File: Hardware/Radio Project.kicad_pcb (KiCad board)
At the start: 10 copper layers, 100 x 70 mm, 110 parts, among them J1 FTSH-105-X-X-DV-007-P-X, J2 USB_C_Receptacle, J3 132225, J4 132225, J5 WE-RJ45_7499010211A, SW1 208-4, U1 STM32F407VGT6, U2 SIT1566AC-JV-XXE-32.768D, U3 ADP2164ACPZ-3.3-R7, U4 SI4468-A2A-IM, U5 SI4468-A2A-IM, U6 DP83822IRHBR, Y1 TG2520SMN 30.0000M-MCGNNM0, Y2 TG2520SMN 30.0000M-MCGNNM0

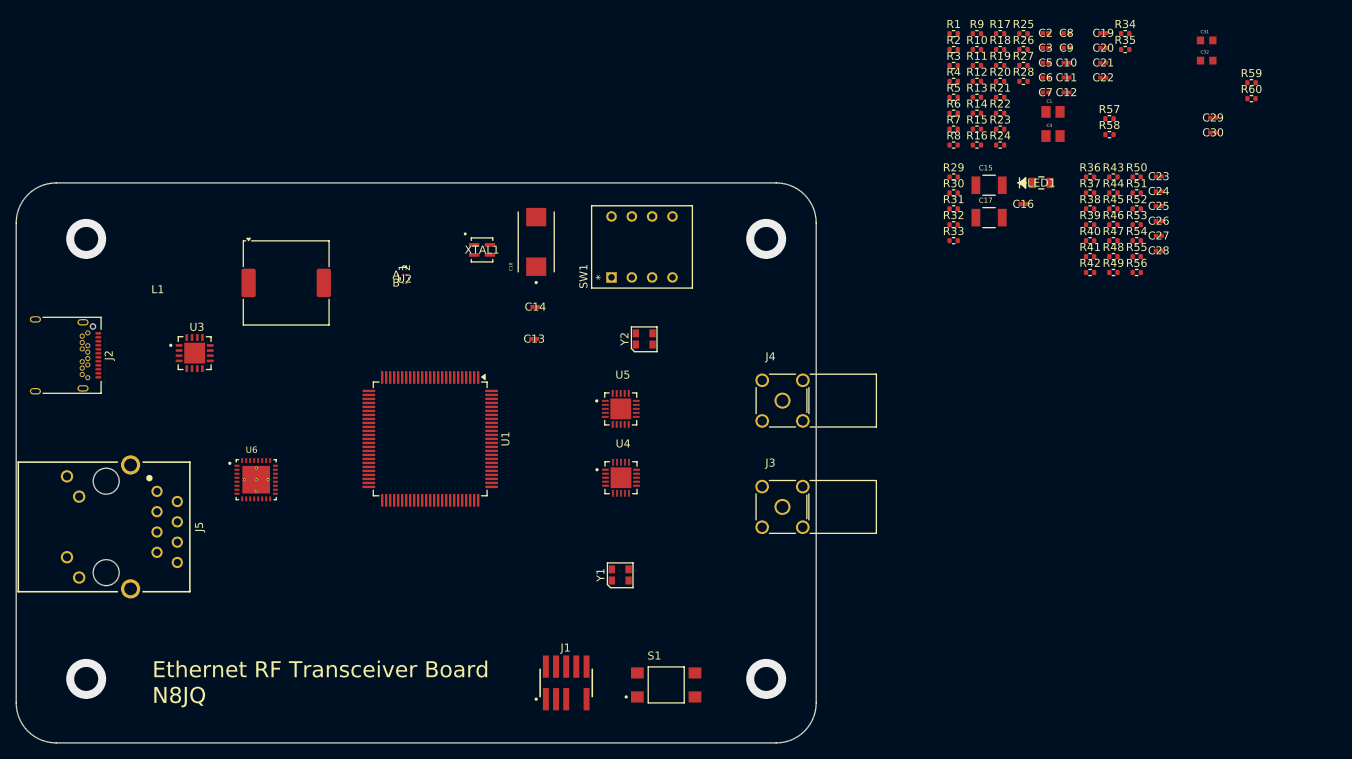
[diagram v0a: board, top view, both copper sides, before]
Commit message: added RF matching network and added all 16 layers to stackup
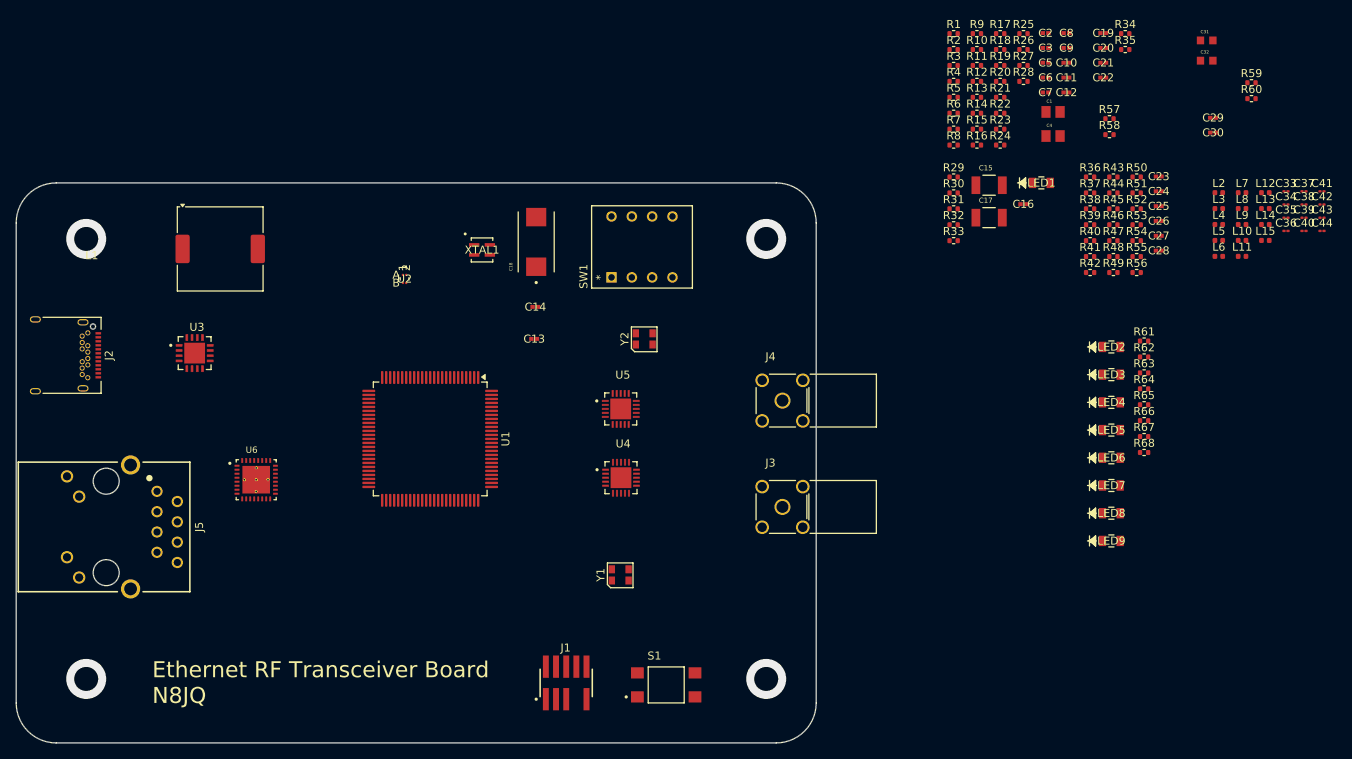
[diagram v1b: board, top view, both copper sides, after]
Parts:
- added C33: 3.3pF, Capacitor_SMD:C_01005_0402Metric, F.Cu at (255.0, 49.0)
- added C34: 3.3pF, Capacitor_SMD:C_01005_0402Metric, F.Cu at (255.0, 50.7)
- added C35: 4.7pF, Capacitor_SMD:C_01005_0402Metric, F.Cu at (255.0, 52.4)
- added C36: 1pF, Capacitor_SMD:C_01005_0402Metric, F.Cu at (255.0, 54.0)
- added C37: 3pF, Capacitor_SMD:C_01005_0402Metric, F.Cu at (257.2, 49.0)
- added C38: 6.2nF, Capacitor_SMD:C_01005_0402Metric, F.Cu at (257.2, 50.7)
- added C39: 3pF, Capacitor_SMD:C_01005_0402Metric, F.Cu at (257.2, 52.4)
- added C40: 4.7pF, Capacitor_SMD:C_01005_0402Metric, F.Cu at (257.2, 54.0)
- added C41: 1pF, Capacitor_SMD:C_01005_0402Metric, F.Cu at (259.5, 49.0)
- added C42: 6.2nF, Capacitor_SMD:C_01005_0402Metric, F.Cu at (259.5, 50.7)
- added C43: 3.3pF, Capacitor_SMD:C_01005_0402Metric, F.Cu at (259.5, 52.4)
- added C44: 3.3pF, Capacitor_SMD:C_01005_0402Metric, F.Cu at (259.5, 54.0)
- added L10: 18nH, Inductor_SMD:L_0402_1005Metric, F.Cu at (249.5, 55.2)
- added L11: 22nH, Inductor_SMD:L_0402_1005Metric, F.Cu at (249.5, 57.2)
- added L12: 3.3nH, Inductor_SMD:L_0402_1005Metric, F.Cu at (252.4, 49.2)
- added L13: 11nH, Inductor_SMD:L_0402_1005Metric, F.Cu at (252.4, 51.2)
- added L14: 22nH, Inductor_SMD:L_0402_1005Metric, F.Cu at (252.4, 53.2)
- added L15: 11nH, Inductor_SMD:L_0402_1005Metric, F.Cu at (252.4, 55.2)
- added L2: 22nH, Inductor_SMD:L_0402_1005Metric, F.Cu at (246.6, 49.2)
- added L3: 11nH, Inductor_SMD:L_0402_1005Metric, F.Cu at (246.6, 51.2)
- added L4: 100nH, Inductor_SMD:L_0402_1005Metric, F.Cu at (246.6, 53.2)
- added L5: 22nH, Inductor_SMD:L_0402_1005Metric, F.Cu at (246.6, 55.2)
- added L6: 18nH, Inductor_SMD:L_0402_1005Metric, F.Cu at (246.6, 57.2)
- added L7: 3.3nH, Inductor_SMD:L_0402_1005Metric, F.Cu at (249.5, 49.2)
- added L8: 11nH, Inductor_SMD:L_0402_1005Metric, F.Cu at (249.5, 51.2)
- added L9: 100nH, Inductor_SMD:L_0402_1005Metric, F.Cu at (249.5, 53.2)
- added LED2: CMD17-21VGD/TR8, CMD17_21VGD_TR8:LED0805N_CML-M, F.Cu at (233.1, 68.5)
- added LED3: CMD17-21VGD/TR8, CMD17_21VGD_TR8:LED0805N_CML-M, F.Cu at (233.1, 72.0)
- added LED4: CMD17-21VGD/TR8, CMD17_21VGD_TR8:LED0805N_CML-M, F.Cu at (233.1, 75.4)
- added LED5: CMD17-21VGD/TR8, CMD17_21VGD_TR8:LED0805N_CML-M, F.Cu at (233.1, 78.9)
- added LED6: CMD17-21VGD/TR8, CMD17_21VGD_TR8:LED0805N_CML-M, F.Cu at (233.1, 82.4)
- added LED7: CMD17-21VGD/TR8, CMD17_21VGD_TR8:LED0805N_CML-M, F.Cu at (233.1, 85.8)
- added LED8: CMD17-21VGD/TR8, CMD17_21VGD_TR8:LED0805N_CML-M, F.Cu at (233.1, 89.3)
- added LED9: CMD17-21VGD/TR8, CMD17_21VGD_TR8:LED0805N_CML-M, F.Cu at (233.1, 92.8)
- added R61: 60, Resistor_SMD:R_0402_1005Metric, F.Cu at (237.2, 67.8)
- added R62: 60, Resistor_SMD:R_0402_1005Metric, F.Cu at (237.2, 69.8)
- added R63: 60, Resistor_SMD:R_0402_1005Metric, F.Cu at (237.2, 71.7)
- added R64: 60, Resistor_SMD:R_0402_1005Metric, F.Cu at (237.2, 73.7)
- added R65: 60, Resistor_SMD:R_0402_1005Metric, F.Cu at (237.2, 75.7)
- added R66: 60, Resistor_SMD:R_0402_1005Metric, F.Cu at (237.2, 77.7)
- added R67: 60, Resistor_SMD:R_0402_1005Metric, F.Cu at (237.2, 79.7)
- added R68: 60, Resistor_SMD:R_0402_1005Metric, F.Cu at (237.2, 81.7)
- moved L1 9.28 mm to (121.8, 56.2)
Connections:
- J3 pad 1: RF1_SMA -> /RF Chain/RF1_SMA
- J4 pad 1: RF2_SMA -> /RF Chain/RF2_SMA
- U1 pad 55: unconnected-(U1-PD8-Pad55) -> Net-(U1-PD8)
- U1 pad 56: unconnected-(U1-PD9-Pad56) -> Net-(U1-PD9)
- U1 pad 83: unconnected-(U1-PD2-Pad83) -> Net-(U1-PD2)
- U1 pad 84: unconnected-(U1-PD3-Pad84) -> Net-(U1-PD3)
- U1 pad 85: unconnected-(U1-PD4-Pad85) -> Net-(U1-PD4)
- U1 pad 86: unconnected-(U1-PD5-Pad86) -> Net-(U1-PD5)
- U1 pad 87: unconnected-(U1-PD6-Pad87) -> Net-(U1-PD6)
- U1 pad 88: unconnected-(U1-PD7-Pad88) -> Net-(U1-PD7)
- U4 pad 2: unconnected-(U4-RXP-Pad2) -> RF1_RX_P
- U4 pad 3: unconnected-(U4-RXN-Pad3) -> RF1_RX_N
- U4 pad 4: unconnected-(U4-TX-Pad4) -> RF1_TX
- U5 pad 2: unconnected-(U5-RXP-Pad2) -> RF2_RX_P
- U5 pad 3: unconnected-(U5-RXN-Pad3) -> RF2_RX_N
- U5 pad 4: unconnected-(U5-TX-Pad4) -> RF2_TX
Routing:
- added copper zone on In1.Cu, net GND
- added copper zone on In10.Cu, net GND
- added copper zone on In12.Cu, net GND
- added copper zone on In14.Cu, net GND
- added copper zone on In3.Cu, net GND
- added copper zone on In8.Cu, net GND
- removed copper zone on In2.Cu, net GND
- removed copper zone on In4.Cu, net GND
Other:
- copper layers 10 -> 16

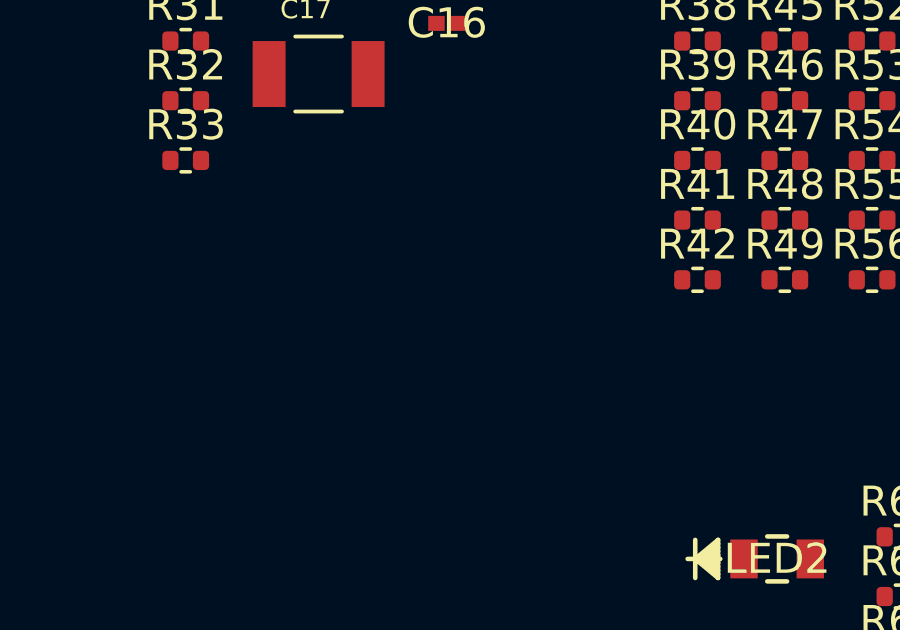
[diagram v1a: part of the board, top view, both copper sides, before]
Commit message: connected USB 2.0 data pins
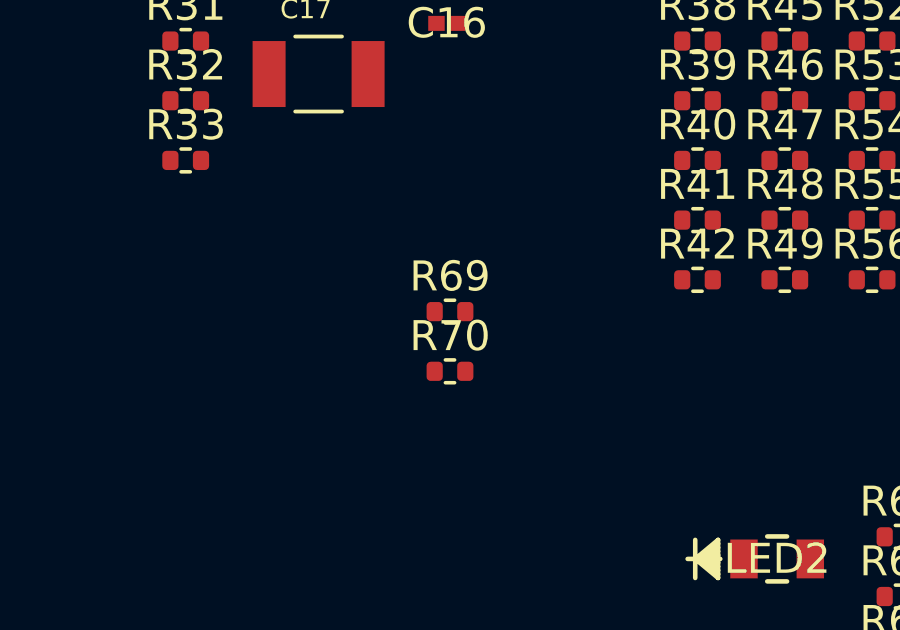
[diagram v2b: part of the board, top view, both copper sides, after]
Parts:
- added R69: 40, Resistor_SMD:R_0402_1005Metric, F.Cu at (222.2, 60.3)
- added R70: 40, Resistor_SMD:R_0402_1005Metric, F.Cu at (222.2, 62.2)
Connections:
- J2 pad A6: unconnected-(J2-D+-PadA6) -> USB_DP
- J2 pad A7: unconnected-(J2-D--PadA7) -> USB_DM
- J2 pad B6: unconnected-(J2-D+-PadB6) -> USB_DM
- J2 pad B7: unconnected-(J2-D--PadB7) -> USB_DP
- U1 pad 70: unconnected-(U1-PA11-Pad70) -> Net-(U1-PA11)
- U1 pad 71: unconnected-(U1-PA12-Pad71) -> Net-(U1-PA12)

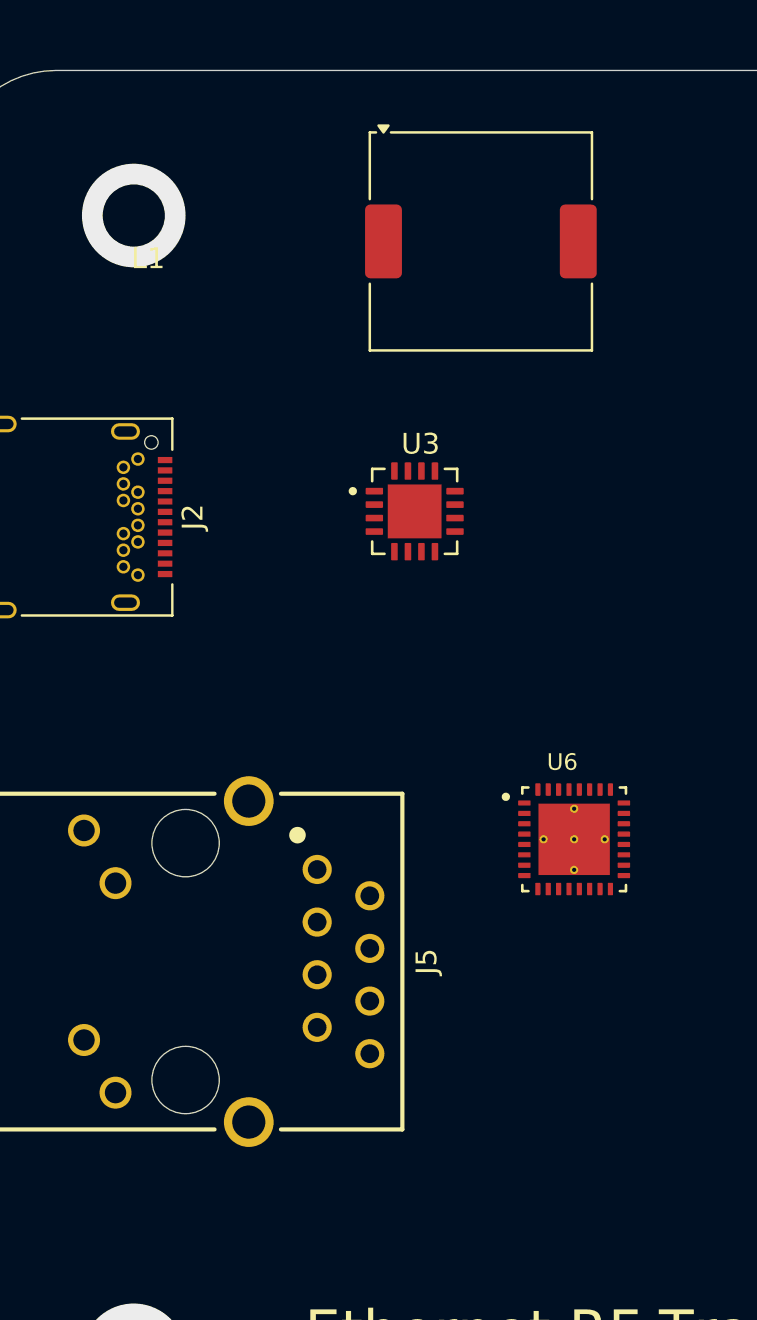
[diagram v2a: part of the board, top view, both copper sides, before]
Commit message: Added 5V plane
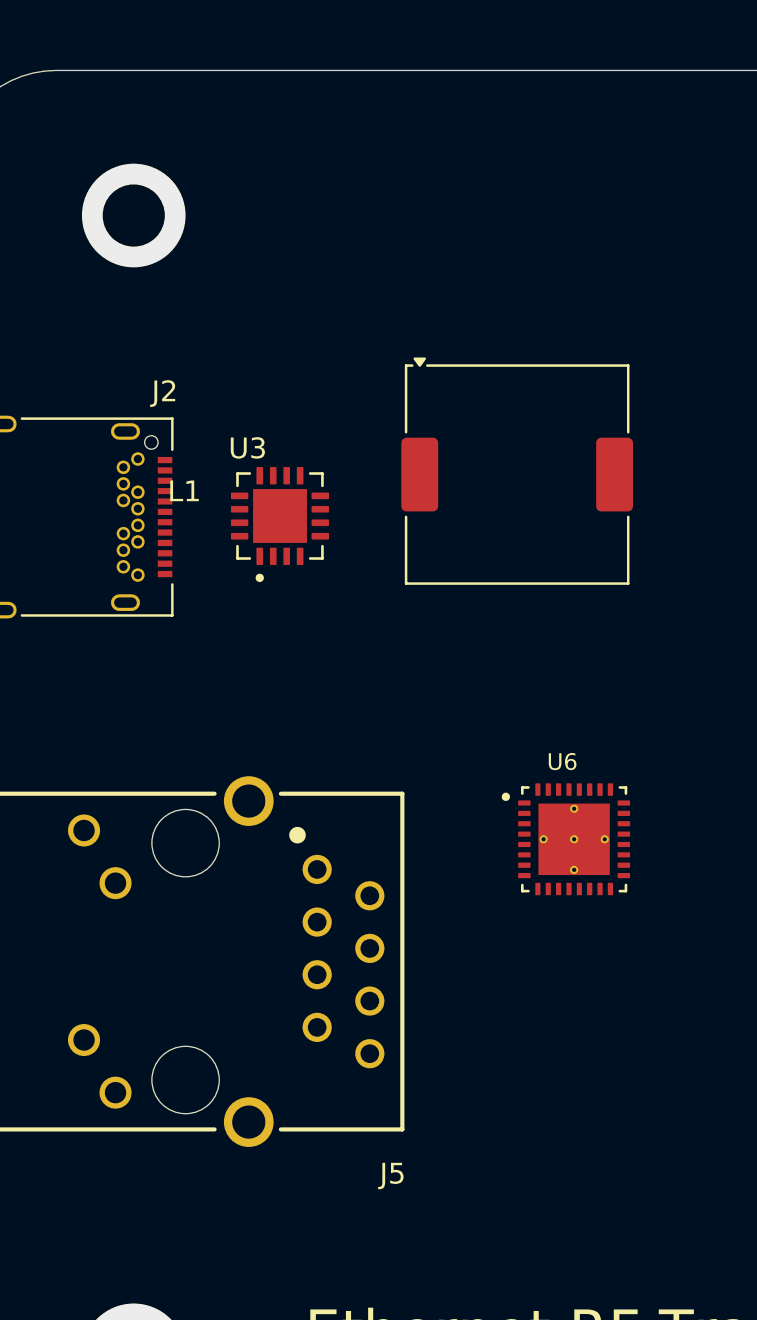
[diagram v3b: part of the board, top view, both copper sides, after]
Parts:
- moved L1 11.4 mm to (123.5, 67.5)
- moved U3 6.50 mm to (112.1, 69.5), turned to 90 degrees
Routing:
- added copper zone on In13.Cu, net +3.3V
- added copper zone on In2.Cu, net +3.3V
- added copper zone on In13.Cu, net +5V
- added copper zone on In2.Cu, net +5V
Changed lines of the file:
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@@
 		(at 107.5 91 -90)
 		(property "Reference" "J5"
-			(at 0 -11.635 90)
+			(at 10.25 -10 180)
 			(layer "F.SilkS")
 			(effects
@@
 		(tags "USB C Type-C Receptacle Hybrid")
 		(property "Reference" "J2"
-			(at 0 -6.36 90)
+			(at -6.05 -5.01 180)
 			(layer "F.SilkS")
 			(effects
@@
 	(footprint "ADP2164ACPZ_3_3_R7:QFN65P400X400X80-17N"
 		(layer "F.Cu")
-		(at 118.555 69.275)
+		(at 112.055 69.5 90)
 		(property "Reference" "U3"
-			(at 0.285 -3.25 0)
+			(at 3.25 -1.555 180)
 			(layer "F.SilkS")
 			(effects
@@
 		)
 		(property "Value" "ADP2164ACPZ-3.3-R7"
-			(at 9.81 3.25 0)
+			(at 9.81 3.25 90)
 			(layer "F.Fab")
 			(effects
@@
 		)
 		(property "Datasheet" ""
-			(at 0 0 0)
+			(at 0 0 90)
 			(layer "F.Fab")
 			(hide yes)
@@
 		)
 		(property "Description" ""
-			(at 0 0 0)
+			(at 0 0 90)
 			(layer "F.Fab")
 			(hide yes)
@@
 		(attr smd)
 		(fp_line
-			(start -2.05 -2.05)
-			(end -2.05 -1.455)
+			(start 2.05 -2.05)
+			(end 1.455 -2.05)
 			(stroke
 				(width 0.127)
@@
 		)
 		(fp_line
-			(start -2.05 -2.05)
-			(end -1.455 -2.05)
+			(start 2.05 -2.05)
+			(end 2.05 -1.455)
 			(stroke
 				(width 0.127)
@@
 		)
 		(fp_line
-			(start -2.05 2.05)
-			(end -2.05 1.455)
+			(start -2.05 -2.05)
+			(end -1.455 -2.05)
 			(stroke
 				(width 0.127)
@@
 		)
 		(fp_line
-			(start -2.05 2.05)
-			(end -1.455 2.05)
+			(start -2.05 -2.05)
+			(end -2.05 -1.455)
 			(stroke
 				(width 0.127)
@@
 		)
 		(fp_line
-			(start 2.05 -2.05)
-			(end 1.455 -2.05)
+			(start 2.05 2.05)
+			(end 2.05 1.455)
 			(stroke
 				(width 0.127)
@@
 		)
 		(fp_line
-			(start 2.05 -2.05)
-			(end 2.05 -1.455)
+			(start 2.05 2.05)
+			(end 1.455 2.05)
 			(stroke
 				(width 0.127)
@@
 		)
 		(fp_line
-			(start 2.05 2.05)
-			(end 1.455 2.05)
+			(start -2.05 2.05)
+			(end -2.05 1.455)
 			(stroke
 				(width 0.127)
@@
 		)
 		(fp_line
-			(start 2.05 2.05)
-			(end 2.05 1.455)
+			(start -2.05 2.05)
+			(end -1.455 2.05)
 			(stroke
 				(width 0.127)
@@
 		)
 		(fp_line
-			(start -2.615 2.615)
-			(end -2.615 -2.615)
+			(start 2.615 2.615)
+			(end 2.615 -2.615)
 			(stroke
 				(width 0.05)
@@
 		(fp_line
 			(start -2.615 2.615)
-			(end 2.615 2.615)
+			(end -2.615 -2.615)
 			(stroke
 				(width 0.05)
@@
 		)
 		(fp_line
-			(start 2.615 2.615)
-			(end 2.615 -2.615)
+			(start -2.615 2.615)
+			(end 2.615 2.615)
 			(stroke
 				(width 0.05)
@@
 		)
 		(fp_line
-			(start -2.05 2.05)
+			(start 2.05 -2.05)
 			(end -2.05 -2.05)
 			(stroke
@@
 		)
 		(fp_line
-			(start 2.05 -2.05)
-			(end -2.05 -2.05)
+			(start 2.05 2.05)
+			(end 2.05 -2.05)
 			(stroke
 				(width 0.127)
@@
 		)
 		(fp_line
-			(start 2.05 2.05)
-			(end 2.05 -2.05)
+			(start -2.05 2.05)
+			(end -2.05 -2.05)
 			(stroke
 				(width 0.127)
@@
 		)
 		(pad "1" smd roundrect
-			(at -1.945 -0.975)
+			(at -1.945 -0.975 90)
 			(size 0.84 0.32)
 			(layers "F.Cu" "F.Mask" "F.Paste")
@@
 		)
 		(pad "2" smd roundrect
-			(at -1.945 -0.325)
+			(at -1.945 -0.325 90)
 			(size 0.84 0.32)
 			(layers "F.Cu" "F.Mask" "F.Paste")
@@
 		)
 		(pad "3" smd roundrect
-			(at -1.945 0.325)
+			(at -1.945 0.325 90)
 			(size 0.84 0.32)
 			(layers "F.Cu" "F.Mask" "F.Paste")
@@
 		)
 		(pad "4" smd roundrect
-			(at -1.945 0.975)
+			(at -1.945 0.975 90)
 			(size 0.84 0.32)
 			(layers "F.Cu" "F.Mask" "F.Paste")
@@
 		)
 		(pad "5" smd roundrect
-			(at -0.975 1.945)
+			(at -0.975 1.945 90)
 			(size 0.32 0.84)
 			(layers "F.Cu" "F.Mask" "F.Paste")
@@
 		)
 		(pad "6" smd roundrect
-			(at -0.325 1.945)
+			(at -0.325 1.945 90)
 			(size 0.32 0.84)
 			(layers "F.Cu" "F.Mask" "F.Paste")
@@
 		)
 		(pad "7" smd roundrect
-			(at 0.325 1.945)
+			(at 0.325 1.945 90)
 			(size 0.32 0.84)
 			(layers "F.Cu" "F.Mask" "F.Paste")
@@
 		)
 		(pad "8" smd roundrect
-			(at 0.975 1.945)
+			(at 0.975 1.945 90)
 			(size 0.32 0.84)
 			(layers "F.Cu" "F.Mask" "F.Paste")
@@
 		)
 		(pad "9" smd roundrect
-			(at 1.945 0.975)
+			(at 1.945 0.975 90)
 			(size 0.84 0.32)
 			(layers "F.Cu" "F.Mask" "F.Paste")
@@
 		)
 		(pad "10" smd roundrect
-			(at 1.945 0.325)
+			(at 1.945 0.325 90)
 			(size 0.84 0.32)
 			(layers "F.Cu" "F.Mask" "F.Paste")
@@
 		)
 		(pad "11" smd roundrect
-			(at 1.945 -0.325)
+			(at 1.945 -0.325 90)
 			(size 0.84 0.32)
 			(layers "F.Cu" "F.Mask" "F.Paste")
@@
 		)
 		(pad "12" smd roundrect
-			(at 1.945 -0.975)
+			(at 1.945 -0.975 90)
 			(size 0.84 0.32)
 			(layers "F.Cu" "F.Mask" "F.Paste")
@@
 		)
 		(pad "13" smd roundrect
-			(at 0.975 -1.945)
+			(at 0.975 -1.945 90)
 			(size 0.32 0.84)
 			(layers "F.Cu" "F.Mask" "F.Paste")
@@
 		)
 		(pad "14" smd roundrect
-			(at 0.325 -1.945)
+			(at 0.325 -1.945 90)
 			(size 0.32 0.84)
 			(layers "F.Cu" "F.Mask" "F.Paste")
@@
 		)
 		(pad "15" smd roundrect
-			(at -0.325 -1.945)
+			(at -0.325 -1.945 90)
 			(size 0.32 0.84)
 			(layers "F.Cu" "F.Mask" "F.Paste")
@@
 		)
 		(pad "16" smd roundrect
-			(at -0.975 -1.945)
+			(at -0.975 -1.945 90)
 			(size 0.32 0.84)
 			(layers "F.Cu" "F.Mask" "F.Paste")
@@
 		)
 		(pad "17" smd rect
-			(at 0 0)
+			(at 0 0 90)
 			(size 2.6 2.6)
 			(layers "F.Cu" "F.Mask")
@@
 	(footprint "Inductor_SMD:L_Coilcraft_MSS1038-XXX"
 		(layer "F.Cu")
-		(at 121.75 56.25)
+		(at 123.5 67.5)
 		(descr "Inductor, Coilcraft, MSS1038-XXX, 10.2x10.0x3.8mm, (https://www.coilcraft.com/getmedia/3e03a7b4-3b1d-4f31-b1f3-e7c621695ac0/mss1038.pdf), generated with kicad-footprint-generator gen_inductor.py")
 		(tags "Inductor mss")
@@
 			)
 		)
+	)
+	(zone
+		(net 17)
+		(net_name "+5V")
+		(layers "In2.Cu" "In13.Cu")
+		(hatch edge 0.5)
+		(connect_pads yes
+			(clearance 0.5)
+		)
+		(min_thickness 0.25)
+		(filled_areas_thickness no)
+		(fill yes
+			(thermal_gap 0.5)
+			(thermal_bridge_width 0.5)
+		)
+		(polygon
+			(pts
+				(xy 95.5 62) (xy 114 62) (xy 114 78) (xy 95.5 78)
+			)
+		)
+	)
+	(zone
+		(net 1)
+		(net_name "+3.3V")
+		(layers "In2.Cu" "In13.Cu")
+		(hatch edge 0.5)
+		(connect_pads yes
+			(clearance 0.5)
+		)
+		(min_thickness 0.25)
+		(filled_areas_thickness no)
+		(fill yes
+			(thermal_gap 0.5)
+			(thermal_bridge_width 0.5)
+		)
+		(polygon
+			(pts
+				(xy 95.5 78) (xy 114 78) (xy 114 62) (xy 95.5 62) (xy 95.5 47) (xy 197.5 47) (xy 197.5 118.5) (xy 95.5 118.5)
+			)
+		)
